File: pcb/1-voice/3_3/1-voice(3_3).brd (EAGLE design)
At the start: 72.6 x 30 mm, 90 parts, among them U1 THAT2180

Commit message: Add LED blink code, Update schem with LED R values
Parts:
- LED1: value (none) -> BLUE
- LED2: value (none) -> RED
- LED3: value (none) -> YELLOW
- LED4: value (none) -> GREEN
- R19: value 1k -> 100k
- R21: value 1k -> 10k
- R22: value 1k -> 470R
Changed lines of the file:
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@@
 <?xml version="1.0" encoding="utf-8"?>
 <!DOCTYPE eagle SYSTEM "eagle.dtd">
-<eagle version="9.2.1">
+<eagle version="9.3.2">
 <drawing>
 <settings>
@@
 <attribute name="SPICEPREFIX" value="C" x="42.3" y="13.8" size="1.778" layer="27" rot="R90" display="off"/>
 </element>
-<element name="LED1" library="led" library_urn="urn:adsk.eagle:library:259" package="1206" package3d_urn="urn:adsk.eagle:package:15796/2" value="" x="10.6" y="26.9" smashed="yes" rot="R270">
+<element name="LED1" library="led" library_urn="urn:adsk.eagle:library:259" package="1206" package3d_urn="urn:adsk.eagle:package:15796/2" value="BLUE" x="10.6" y="26.9" smashed="yes" rot="R270">
 <attribute name="VALUE" x="8.06" y="28.17" size="1.27" layer="27" rot="R270"/>
 </element>
-<element name="LED2" library="led" library_urn="urn:adsk.eagle:library:259" package="1206" package3d_urn="urn:adsk.eagle:package:15796/2" value="" x="6.2" y="26.9" smashed="yes" rot="R270">
+<element name="LED2" library="led" library_urn="urn:adsk.eagle:library:259" package="1206" package3d_urn="urn:adsk.eagle:package:15796/2" value="RED" x="6.2" y="26.9" smashed="yes" rot="R270">
 <attribute name="VALUE" x="3.66" y="28.17" size="1.27" layer="27" rot="R270"/>
 </element>
-<element name="LED3" library="led" library_urn="urn:adsk.eagle:library:259" package="1206" package3d_urn="urn:adsk.eagle:package:15796/2" value="" x="8.4" y="26.9" smashed="yes" rot="R90">
+<element name="LED3" library="led" library_urn="urn:adsk.eagle:library:259" package="1206" package3d_urn="urn:adsk.eagle:package:15796/2" value="YELLOW" x="8.4" y="26.9" smashed="yes" rot="R90">
 <attribute name="VALUE" x="10.94" y="25.63" size="1.27" layer="27" rot="R90"/>
 </element>
-<element name="R19" library="rcl" library_urn="urn:adsk.eagle:library:334" package="R0603" package3d_urn="urn:adsk.eagle:package:23555/3" value="1k" x="10.6" y="22.9" smashed="yes" rot="R90">
+<element name="R19" library="rcl" library_urn="urn:adsk.eagle:library:334" package="R0603" package3d_urn="urn:adsk.eagle:package:23555/3" value="100k" x="10.6" y="22.9" smashed="yes" rot="R90">
 <attribute name="SPICEPREFIX" value="R" x="10.6" y="22.9" size="1.778" layer="27" rot="R90" display="off"/>
 </element>
@@
 <attribute name="SPICEPREFIX" value="R" x="6.2" y="22.9" size="1.778" layer="27" rot="R90" display="off"/>
 </element>
-<element name="R21" library="rcl" library_urn="urn:adsk.eagle:library:334" package="R0603" package3d_urn="urn:adsk.eagle:package:23555/3" value="1k" x="8.4" y="22.9" smashed="yes" rot="R90">
+<element name="R21" library="rcl" library_urn="urn:adsk.eagle:library:334" package="R0603" package3d_urn="urn:adsk.eagle:package:23555/3" value="10k" x="8.4" y="22.9" smashed="yes" rot="R90">
 <attribute name="SPICEPREFIX" value="R" x="8.4" y="22.9" size="1.778" layer="27" rot="R90" display="off"/>
 </element>
-<element name="LED4" library="led" library_urn="urn:adsk.eagle:library:259" package="1206" package3d_urn="urn:adsk.eagle:package:15796/2" value="" x="4" y="26.9" smashed="yes" rot="R270">
+<element name="LED4" library="led" library_urn="urn:adsk.eagle:library:259" package="1206" package3d_urn="urn:adsk.eagle:package:15796/2" value="GREEN" x="4" y="26.9" smashed="yes" rot="R270">
 <attribute name="VALUE" x="1.46" y="28.17" size="1.27" layer="27" rot="R270"/>
 </element>
-<element name="R22" library="rcl" library_urn="urn:adsk.eagle:library:334" package="R0603" package3d_urn="urn:adsk.eagle:package:23555/3" value="1k" x="4" y="22.9" smashed="yes" rot="R90">
+<element name="R22" library="rcl" library_urn="urn:adsk.eagle:library:334" package="R0603" package3d_urn="urn:adsk.eagle:package:23555/3" value="470R" x="4" y="22.9" smashed="yes" rot="R90">
 <attribute name="SPICEPREFIX" value="R" x="4" y="22.9" size="1.778" layer="27" rot="R90" display="off"/>
 </element>

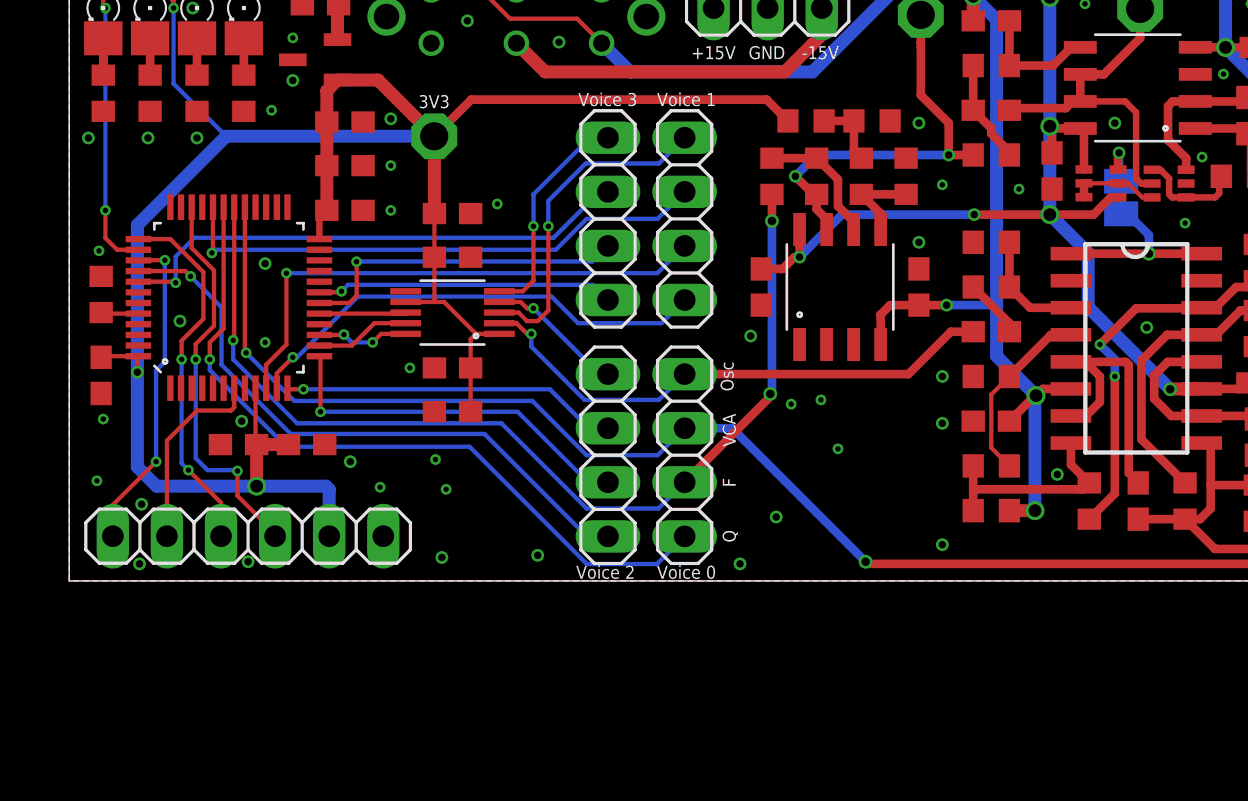
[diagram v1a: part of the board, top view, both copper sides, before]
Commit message: Found error in sch values around lin->exp converter
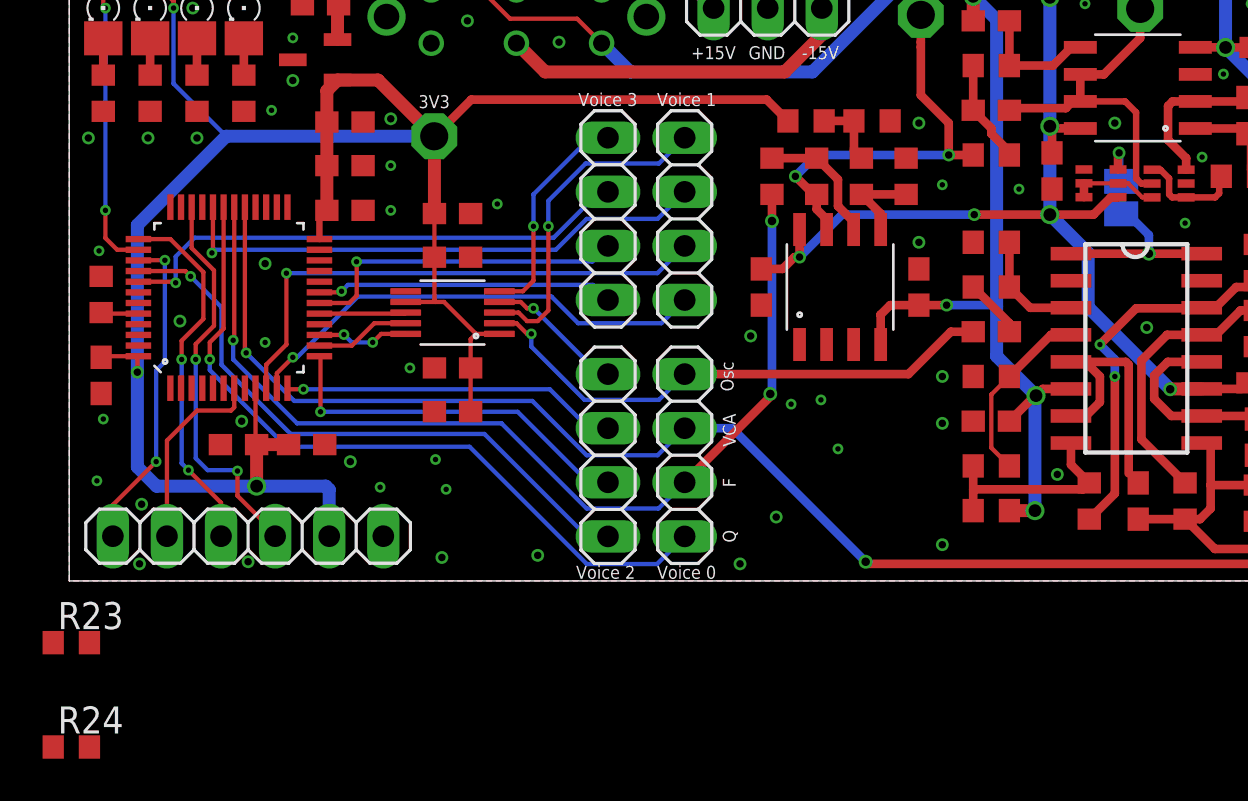
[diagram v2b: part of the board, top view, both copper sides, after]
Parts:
- added R23, R24: 1k, rcl:R0603
- C20: value 10u -> 10p
- R9: value 2.7M -> 845k
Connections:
- new net N$23: Q2.4, R23.1
- new net N$24: Q2.1, R24.1
- net +15V: now also R23.2, R24.2; no longer Q2.1, Q2.4
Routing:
- net +15V: track 139.7 -> 137.9 mm
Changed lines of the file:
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@@
 <?xml version="1.0" encoding="utf-8"?>
 <!DOCTYPE eagle SYSTEM "eagle.dtd">
-<eagle version="9.3.2">
+<eagle version="9.2.1">
 <drawing>
 <settings>
@@
 <attribute name="SPICEPREFIX" value="R" x="58.1" y="3.65" size="1.778" layer="27" rot="R270" display="off"/>
 </element>
-<element name="U$11" library="synth" package="SOIC8" value="TL072" x="52.58" y="23.15" smashed="yes" rot="R90"/>
+<element name="U$11" library="synth" package="SOIC8" value="TL072" x="52.58" y="23.15" smashed="yes" rot="R90">
+<attribute name="SPICEPREFIX" value="U" x="52.58" y="23.15" size="1.778" layer="27" rot="R90" display="off"/>
+</element>
 <element name="C18" library="rcl" library_urn="urn:adsk.eagle:library:334" package="C0603" package3d_urn="urn:adsk.eagle:package:23616/2" value="0.1u" x="58.6" y="9.3" smashed="yes" rot="R180">
 <attribute name="SPICEPREFIX" value="C" x="58.6" y="9.3" size="1.778" layer="27" rot="R180" display="off"/>
@@
 </element>
 <element name="Q1" library="LITTLEBITS" package="SOT-363-JBLMASK" value="" x="54.05" y="18.66" smashed="yes" rot="R270">
+<attribute name="SPICEPREFIX" value="Q" x="54.05" y="18.66" size="1.778" layer="27" rot="R270" display="off"/>
 <attribute name="VALUE" x="51.985" y="19.76" size="0.4064" layer="27" font="vector" rot="R270"/>
 </element>
 <element name="Q2" library="LITTLEBITS" package="SOT-363-JBLMASK" value="" x="50.85" y="18.67" smashed="yes" rot="R270">
+<attribute name="SPICEPREFIX" value="Q" x="50.85" y="18.67" size="1.778" layer="27" rot="R270" display="off"/>
 <attribute name="VALUE" x="48.785" y="19.77" size="0.4064" layer="27" font="vector" rot="R270"/>
 </element>
@@
 <attribute name="SPICEPREFIX" value="R" x="57.35" y="19" size="1.778" layer="27" rot="R180" display="off"/>
 </element>
-<element name="C20" library="rcl" library_urn="urn:adsk.eagle:library:334" package="C0603" package3d_urn="urn:adsk.eagle:package:23616/2" value="10u" x="57.7" y="21.85" smashed="yes" rot="R270">
+<element name="C20" library="rcl" library_urn="urn:adsk.eagle:library:334" package="C0603" package3d_urn="urn:adsk.eagle:package:23616/2" value="10p" x="57.7" y="21.85" smashed="yes" rot="R270">
 <attribute name="SPICEPREFIX" value="C" x="57.7" y="21.85" size="1.778" layer="27" rot="R270" display="off"/>
 </element>
-<element name="R9" library="rcl" library_urn="urn:adsk.eagle:library:334" package="R0603" package3d_urn="urn:adsk.eagle:package:23555/3" value="2.7M" x="59.8" y="21.85" smashed="yes" rot="R270">
+<element name="R9" library="rcl" library_urn="urn:adsk.eagle:library:334" package="R0603" package3d_urn="urn:adsk.eagle:package:23555/3" value="845k" x="59.8" y="21.85" smashed="yes" rot="R270">
 <attribute name="SPICEPREFIX" value="R" x="59.8" y="21.85" size="1.778" layer="27" rot="R270" display="off"/>
 </element>
@@
 <element name="U$6" library="synth" package="DPDT" value="SWITCH-DPDT" x="23.4" y="26.5" smashed="yes" rot="R180"/>
 <element name="SJ1" library="jumper" library_urn="urn:adsk.eagle:library:252" package="SJ" package3d_urn="urn:adsk.eagle:package:15471/1" value="" x="51.8" y="18" smashed="yes" rot="MR90">
+<attribute name="SPICEPREFIX" value="B" x="51.8" y="18" size="1.778" layer="28" rot="MR90" display="off"/>
 <attribute name="VALUE" x="51.8" y="18.4001" size="0.02" layer="28" rot="MR90"/>
+</element>
+<element name="R23" library="rcl" library_urn="urn:adsk.eagle:library:334" package="R0603" package3d_urn="urn:adsk.eagle:package:23555/3" value="1k" x="2.5" y="-2.9" smashed="yes">
+<attribute name="NAME" x="1.865" y="-2.265" size="1.27" layer="25"/>
+<attribute name="SPICEPREFIX" value="R" x="2.5" y="-2.9" size="1.778" layer="27" display="off"/>
+<attribute name="VALUE" x="1.865" y="-4.805" size="1.27" layer="27"/>
+</element>
+<element name="R24" library="rcl" library_urn="urn:adsk.eagle:library:334" package="R0603" package3d_urn="urn:adsk.eagle:package:23555/3" value="1k" x="2.5" y="-7.8" smashed="yes">
+<attribute name="NAME" x="1.865" y="-7.165" size="1.27" layer="25"/>
+<attribute name="SPICEPREFIX" value="R" x="2.5" y="-7.8" size="1.778" layer="27" display="off"/>
+<attribute name="VALUE" x="1.865" y="-9.705" size="1.27" layer="27"/>
 </element>
 </elements>
@@
 <contactref element="C18" pad="2"/>
 <contactref element="R9" pad="2"/>
-<contactref element="Q2" pad="4"/>
-<contactref element="Q2" pad="1"/>
 <contactref element="U$4" pad="P$2"/>
 <contactref element="C21" pad="1"/>
@@
 <wire x1="67.5" y1="20.8" x2="67.5" y2="21.975" width="0.6096" layer="1"/>
 <wire x1="67.5" y1="21.975" x2="67.71" y2="22.185" width="0.6096" layer="1"/>
-<wire x1="50.05" y1="19.32" x2="50.05" y2="21.075" width="0.4064" layer="1"/>
 <wire x1="50.05" y1="21.075" x2="49.88" y2="21.245" width="0.2032" layer="1"/>
-<wire x1="51.65" y1="18.02" x2="51.63" y2="18" width="0.2032" layer="1"/>
 <wire x1="51.63" y1="18" x2="51.3" y2="18" width="0.4064" layer="1"/>
 <wire x1="51.3" y1="18" x2="50.5" y2="17.2" width="0.4064" layer="1"/>
@@
 <via x="44.9" y="17.2" extent="1-16" drill="0.35"/>
 <wire x1="44.9" y1="17.2" x2="48.45" y2="17.2" width="0.4064" layer="1"/>
+<contactref element="R23" pad="2"/>
+<contactref element="R24" pad="2"/>
+<wire x1="3.35" y1="-2.9" x2="15" y2="25.42" width="0" layer="19" extent="1-1"/>
+<wire x1="3.35" y1="-7.8" x2="3.35" y2="-2.9" width="0" layer="19" extent="1-1"/>
 </signal>
 <signal name="OSC1-OUT">
@@
 <wire x1="51.7" y1="18.862" x2="51.8" y2="18.762" width="0.4064" layer="16"/>
 </signal>
+<signal name="N$23">
+<contactref element="R23" pad="1"/>
+<contactref element="Q2" pad="4"/>
+<wire x1="1.65" y1="-2.9" x2="51.65" y2="18.02" width="0" layer="19" extent="1-1"/>
+</signal>
+<signal name="N$24">
+<contactref element="R24" pad="1"/>
+<contactref element="Q2" pad="1"/>
+<wire x1="1.65" y1="-7.8" x2="50.05" y2="19.32" width="0" layer="19" extent="1-1"/>
+</signal>
 </signals>

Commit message: Changed board rails, transferred sims to pcb
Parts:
- removed TP5: TPPAD1-13, testpad:P1-13
- removed U$2: STM32C8, synth:LQFP48
- added C27: 2000p, rcl:C0603
- added C28: 1000p, rcl:C0603
- added C29, C30, C31, C32, C33, C34: 0.1u, rcl:C0603
- added D1, D2, D3, D4, D5, D6: 1N4148, LITTLEBITS:SOD123
- added Q3, Q4: (no value), LITTLEBITS:SOT-363-JBLMASK
- added R25, R45: 30k, rcl:R0603
- added R28: 562k, rcl:R0603
- added R37, R43, R44: 10k, rcl:R0603
- added R38: 3.3k, rcl:R0603
- added R39: 100k, rcl:R0603
- added R40: 14.7k, rcl:R0603
- added R41: 1.6k, rcl:R0603
- added R42: 8.45k, rcl:R0603
- added R46: 10, rcl:R0603
- added SJ2: (no value), jumper:SJ
- added TP1, TP2: TPPAD1-13, testpad:P1-13
- added U11, U12, U5, U7: TL072, synth:SOIC8
- added U8: (no value), LITTLEBITS:DMP16
- added VR1, VR2: 1k, LITTLEBITS:POT-TRIM-SMD-BOURNS-3314
- C1: value 0.1u -> 10p
- C3: value 0.1u -> 1000p
- C4: value 22p -> 2000p
- C42: value 1000p -> 2200p
- C43: value 2000p -> 2200p
- C7: value 1000p -> 0.1u
- C8: value 2000p -> 0.1u
- R1: value 22k -> 3.5k
- R10: value 20k -> 10k
- R13: value 330k -> 165k
- R14: value 5.1k -> 1k
- R15: value 20k -> 570
- R16: value 330k -> 72k
- R17: value 4.7k -> 570
- R18: value 4.7k -> 72k
- R2: value 22k -> 30k
- R23, R24: value 1k -> 10
- R26, R33, R35: value 100k -> 10k
- R27, R30, R32, R34: value 2k -> 220
- R29: value 100K -> 10k
- R3: value 4.7k -> 10k
- R31: value 10k -> 10
- R36: value 10k -> 3.3k
- R4: value 1k -> 10k
- R6: value 10k -> 165k
- R9: value 845k -> 280k
- U$1: value TL072 -> TRS; device synth:SOIC8 -> synth:TRS
- U1: value THAT2180 -> STM32C8; device synth:SIP8 -> synth:LQFP48
- moved U$1 244.0 mm to (-31.8, -197.5), turned to 0 degrees
- moved C8 232.3 mm to (-30.9, -189.9), turned to 0 degrees
- moved C7 231.7 mm to (-30.9, -185.0)
- moved R5 221.5 mm to (-30.9, -180.1), turned to 0 degrees
- moved C4 217.1 mm to (-30.9, -170.3)
- moved R6 213.7 mm to (-24.5, -170.3), turned to 0 degrees
- moved R3 213.2 mm to (-26.2, -175.2)
- moved R4 209.5 mm to (-21.9, -175.2)
- moved R18 208.2 mm to (-30.9, -175.2), turned to 0 degrees
- moved C3 201.7 mm to (-25.8, -163.2), turned to 0 degrees
- moved R17 200.9 mm to (-19.2, -170.3), turned to 0 degrees
- moved R14 193.1 mm to (-30.9, -150.0), turned to 0 degrees
- moved C1 191.7 mm to (-26.2, -154.9), turned to 0 degrees
- moved R2 187.5 mm to (-30.9, -137.9)
- moved R31 169.3 mm to (-26.2, -150.0)
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- renumbered U$10 to U6, U$11 to U9, U$3 to U2, U$4 to U3, U$5 to U4
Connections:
- removed net N$3: C4.1, R2.1, U$1.P$2, U1.$P8
- removed net VCA_OUT0: C4.2, R2.2, TP4.TP, U$1.P$1
- new net N$25: C43.1, U6.12, U7.P$5
- new net N$26: R36.2, U8.5, U9.P$5
- new net N$28: C42.1, U6.5, U7.P$3
- new net N$29: R25.1, U8.3, VR1.1
- new net N$30: U8.4, VR1.3
- new net N$37: D2.C, D3.A
- new net N$38: D1.C, D2.A
- new net N$39: D4.C, D5.A
- new net N$40: D5.C, D6.A
- new net N$41: R40.1, R41.2, R42.1
- new net N$42: R39.1, R40.2, U5.P$2
- new net N$43: R39.2, R43.1, U5.P$1
- new net N$44: C27.1, R43.2, R44.1
- new net N$45: C28.1, R44.2, U5.P$5
- new net N$46: R45.1, U8.1
- new net N$47: U8.13, VR2.3
- new net N$48: C1.1, Q3.6, R28.1, U11.P$6
- new net N$49: R29.2, R33.1, U7.P$1, U7.P$2
- new net N$50: R17.1, R18.2, U12.P$5
- new net N$51: Q3.3, Q4.2, Q4.3, Q4.5
- new net N$52: Q4.6, SJ2.2
- new net N$53: Q4.4, R31.1
- new net N$54: Q4.1, R46.1
- new net Q-CTRL0-I: C27.2, R45.2, U5.P$6, U5.P$7
- new net VCA-OUT0: R1.1, TP4.TP, U$1.P$2, U11.P$1
- new net VCA0-EXP: SJ2.1, U8.16
- net +15V: now also C29.1, C31.2, C33.1, C8.2, R16.1, R18.1, R28.2, R31.2, R42.2, R46.2, U11.P$8, U12.P$8, U5.P$8, U7.P$8, U8.11; no longer C3.2, U$1.P$8, U1.$P7
- net +3V3: now also U1.P$24, U1.P$48, U1.P$9; no longer R18.2, U$2.P$24, U$2.P$48, U$2.P$9
- net -15V: now also C28.2, C3.2, C30.2, C32.1, C34.2, U11.P$4, U12.P$4, U5.P$4, U7.P$4, U8.6; no longer C1.1, R14.1, R31.2, R36.2, U$1.P$4
- net F-CTRL0: now also R6.2, U1.P$30; no longer U$2.P$30
- net F-CTRL0-LIN: now also U4.P$1, U4.P$2; no longer U9.P$6, U9.P$7
- net F-CTRL1: now also U1.P$10; no longer U$2.P$10
- net F-CTRL2: now also U1.P$13; no longer U$2.P$13
- net F-CTRL3: now also U1.P$18; no longer U$2.P$18
- net F0-OUT: now also R2.1, R2.2, R25.2, R35.2, U7.P$6, U7.P$7, U8.14, VR2.1; no longer C42.2, R1.1, R35.1, R36.1, U6.9
- net GND: now also C29.2, C30.1, C31.1, C32.2, C33.2, C34.1, C7.2, C8.1, Q3.5, R17.2, R36.1, R38.1, R41.1, U$1.P$1, U1.P$23, U1.P$47, U1.P$8, U11.P$3, U11.P$5, VR1.2, VR2.2; no longer C1.2, C3.1, R17.1, R4.1, U$1.P$3, U$2.P$23, U$2.P$47, U$2.P$8, U1.$P2, U1.$P6
- net LED: now also U1.P$38; no longer U$2.P$38
- net MOSI: now also U1.P$17; no longer U$2.P$17
- net N$12: now also U4.P$3; no longer U9.P$5
- net N$16: now also Q3.1, Q3.4; no longer U1.$P5
- net N$19: now also R5.2, R6.1, U12.P$6; no longer R16.1, R17.2, R18.1
- net N$2: now also U11.P$2, U8.12; no longer U1.$P1
- net N$31: now also R29.1; no longer R29.2
- net N$32: now also D1.A, D6.C, R37.1, R38.2, U9.P$6; no longer C42.1, U6.5, U6.7
- net N$33: now also C1.2, R14.1, U11.P$7; no longer R29.1, R31.1, R33.1, U6.8
- net N$34: now also C42.2, D3.C, D4.A, R37.2, U9.P$7; no longer C43.1, U6.10, U6.12
- net N$36: now also R35.1; no longer R35.2
- net N$4: now also C3.1, U12.P$3; no longer R4.2, R5.2
- net N$5: now also C4.1, R3.1, R4.2; no longer C8.2, R5.1, R6.2
- net N$6: now also R4.1, R5.1, TP2.TP, U12.P$7; no longer C7.2, R6.1, U$1.P$5
- net N$8: now also U1.P$44; no longer U$2.P$44
- net NRST: now also U1.P$7; no longer U$2.P$7
- net NSS: now also U1.P$14; no longer U$2.P$14
- net Q-CTRL0: now also U1.P$31, U5.P$3; no longer U$2.P$31
- net Q-CTRL1: now also U1.P$11; no longer U$2.P$11
- net Q-CTRL2: now also U1.P$40; no longer U$2.P$40
- net Q-CTRL3: now also U1.P$19; no longer U$2.P$19
- net SCK: now also U1.P$15; no longer U$2.P$15
- net SWCLK: now also U1.P$37; no longer U$2.P$37
- net SWDIO: now also U1.P$34; no longer U$2.P$34
- net SWO: now also U1.P$39; no longer U$2.P$39
- net VCA-CTRL0: now also U1.P$29; no longer R3.1, U$2.P$29
- net VCA-CTRL1: now also U1.P$32; no longer U$2.P$32
- net VCA-CTRL2: now also U1.P$12; no longer U$2.P$12
- net VCA-CTRL3: now also U1.P$41; no longer U$2.P$41
- net VCA0-LP: now also C4.2, Q3.2, TP1.TP, U12.P$1, U12.P$2; no longer C8.1, TP5.TP, U$1.P$6, U$1.P$7, U1.$P3
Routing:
- net VCA0-LP: track 28.5 -> 0.00 mm, vias 2 -> 0
- net F0-OUT: track 23.4 -> 2.63 mm
- net N$32: track 12.3 -> 0.00 mm
- net N$3: track 10.4 -> 0.00 mm
- net N$33: track 9.91 -> 0.00 mm
- net N$34: track 8.74 -> 0.00 mm
- net VCA_OUT0: track 6.47 -> 0.00 mm
- net -15V: track 164.7 -> 159.4 mm
- net +15V: track 137.9 -> 133.0 mm
- net N$5: track 4.90 -> 0.00 mm
- net N$4: track 4.90 -> 0.00 mm
- net F-CTRL0-LIN: track 16.4 -> 11.6 mm
- net N$6: track 4.82 -> 0.00 mm
- net N$19: track 3.29 -> 0.00 mm
- net N$16: track 3.20 -> 0.00 mm
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
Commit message: Standardize part vals
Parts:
- removed TP8: TPPAD1-13, testpad:P1-13
- removed U$1: TRS, synth:TRS
- added JP2: (no value), pinhead:1X03
- added TP5: TPPAD1-13, testpad:P1-13
- C35, C36: value 2200p -> 2000p
- C9: value .01u -> 0.01u
- JP7: value (none) -> TRS; device pinhead:1X03 -> synth:TRS
- Q1, Q3: value (none) -> BC847BS
- Q2, Q4: value (none) -> BC857BS
- R1: value 3.5k -> 3.48k
- R15, R17: value 570 -> 562
- R41: value 1.6k -> 1.62k
- U6, U8: value (none) -> LM13700
- moved JP7 234.2 mm to (-31.8, -197.5), turned to 0 degrees
- moved TP6 26.3 mm to (52.7, 26.9)
- moved TP7 10.3 mm to (42.4, 26.6)
- renumbered C42 to C35, C43 to C36, C44 to C37, C45 to C38, JP10 to JP5, JP11 to JP6, JP8 to JP3, JP9 to JP4, U$6 to SW1, U12 to U10
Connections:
- net +15V renamed +12V
- net -15V renamed -12V
- new net N$3: R2.2, U8.14, VR2.1
- net -15V-IN: now also JP2.1; no longer JP7.1
- net 15V-IN: now also JP2.3; no longer JP7.3
- net F-CTRL0-LIN: now also TP6.TP; no longer TP7.TP
- net F0-OUT: now also TP5.TP; no longer R2.2, TP6.TP, U8.14, VR2.1
- net GND: now also JP2.2, JP7.P$1; no longer JP7.2, U$1.P$1
- net N$15: now also TP7.TP; no longer TP8.TP
- net VCA-OUT0: now also JP7.P$2; no longer U$1.P$2
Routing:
- net +12V: track 133.0 -> 120.5 mm
- net -12V: track 159.4 -> 155.2 mm
